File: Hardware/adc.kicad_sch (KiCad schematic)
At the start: 18 parts, among them U2 ADS1256IDBT, Y1 8MHz

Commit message: Version 0.1
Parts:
- removed R10, R12, R14, R15, R9: 100, Resistor_SMD:R_0805_2012Metric_Pad1.20x1.40mm_HandSolder, symbol Device:R
- removed R11, R13: 0, Resistor_SMD:R_0805_2012Metric_Pad1.20x1.40mm_HandSolder, symbol Device:R
- removed R7, R8: 10k, Resistor_SMD:R_0805_2012Metric_Pad1.20x1.40mm_HandSolder, symbol Device:R
- removed U2: ADS1256IDBT, ADS1256IDBT:SOP65P780X200-28N, symbol ADS1256:ADS1256IDBT
- removed Y1: 8MHz, Crystal:Crystal_SMD_3225-4Pin_3.2x2.5mm_HandSoldering, symbol Device:Crystal
- added U2: NAU7802SGI, symbol Nuvoton_-_NAU7802SGI:NAU7802SGI
- C10: value 18p -> 0.1uF; footprint Capacitor_SMD:C_0805_2012Metric_Pad1.18x1.45mm_HandSolder -> Capacitor_SMD:C_0603_1608Metric_Pad1.08x0.95mm_HandSolder
- C6: value 22u -> 1uF; footprint Capacitor_SMD:C_0805_2012Metric_Pad1.18x1.45mm_HandSolder -> Capacitor_SMD:C_0603_1608Metric_Pad1.08x0.95mm_HandSolder
- C7: value 100n -> 0.1uF; footprint Capacitor_SMD:C_0805_2012Metric_Pad1.18x1.45mm_HandSolder -> Capacitor_SMD:C_0603_1608Metric_Pad1.08x0.95mm_HandSolder
- C8: value 100p -> 0.1uF; footprint Capacitor_SMD:C_0805_2012Metric_Pad1.18x1.45mm_HandSolder -> Capacitor_SMD:C_0603_1608Metric_Pad1.08x0.95mm_HandSolder
- C9: value 18p -> 470pF; footprint Capacitor_SMD:C_0805_2012Metric_Pad1.18x1.45mm_HandSolder -> Capacitor_SMD:C_0603_1608Metric_Pad1.08x0.95mm_HandSolder
- R5, R6: value 49.9 -> 51; footprint Resistor_SMD:R_0805_2012Metric_Pad1.20x1.40mm_HandSolder -> Resistor_SMD:R_0603_1608Metric_Pad0.98x0.95mm_HandSolder
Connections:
- net +2V5 is gone; now on net AIN+: R5.1
- net +3V3: now also U2.15 (DVDD)
- net AIN-: now also R6.1
- net GND: now also C10.1, C6.1, C7.1, U2.7 (REFN), U2.8 (AVSS), U2.9 (DVSS); no longer C10.2, C9.1, R6.1
- net at C8.1, R5.2: now also U2.3 (VIN1P); no longer C6.1, C7.1
- net at C9.2: now also U2.4 (VIN2N)
- net at C6.2, C7.2: now also U2.1 (REFP); no longer C8.2, R6.2
- new net: C10.2, U2.6 (VBG)
- new net: C8.2, R6.2, U2.2 (VIN1N)
- new net: C9.1, U2.5 (VIN2P)
- new net SCL: U2.13 (SCLK)
- new net SDA: U2.14 (SDIO)
- no-connect marks 10 -> 0

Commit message: Readme + hole update
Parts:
- U2: footprint (none) -> Nuvoton-NAU7802SGI:Nuvoton-NAU7802SGI
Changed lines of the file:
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@@
     (property "Reference" "U2" (id 0) (at 157.48 90.17 0))
     (property "Value" "NAU7802SGI" (id 1) (at 157.48 92.71 0))
-    (property "Footprint" "" (id 2) (at 139.7 87.63 0)
+    (property "Footprint" "Nuvoton-NAU7802SGI:Nuvoton-NAU7802SGI" (id 2) (at 139.7 87.63 0)
       (effects (font (size 1.27 1.27)) (justify left) hide)
     )

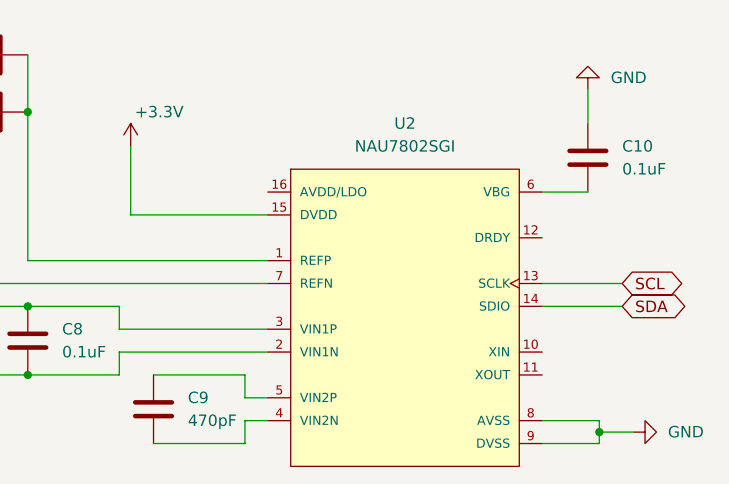
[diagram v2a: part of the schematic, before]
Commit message: removed TP561023, added footprint libraries
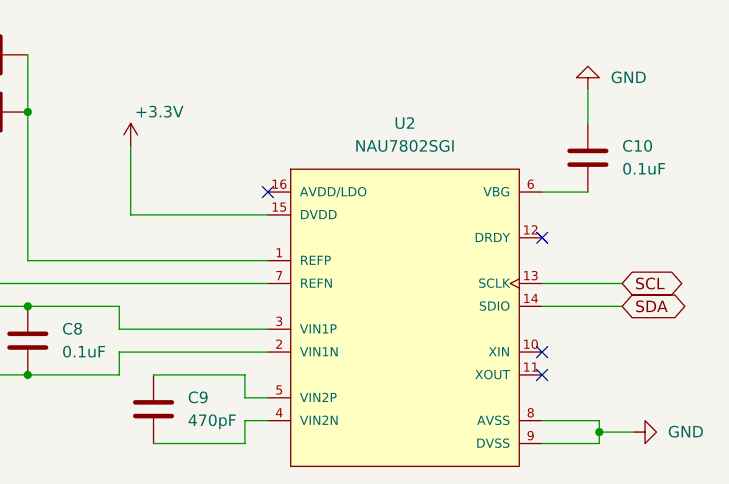
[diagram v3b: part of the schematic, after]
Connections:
- no-connect marks 0 -> 4
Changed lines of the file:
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@@
   (junction (at 107.95 82.55) (diameter 0) (color 0 0 0 0)
   )
+  (no_connect (at 172.72 102.87))
+  (no_connect (at 142.24 97.79))
+  (no_connect (at 172.72 118.11))
+  (no_connect (at 172.72 115.57))
   (wire (pts (xy 100.33 72.39) (xy 107.95 72.39))
     (stroke (width 0) (type default) (color 0 0 0 0))

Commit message: Updated power design
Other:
- note added: "This is 51ohms in Adafruits implementation"
- note added: "This was 0.1uF in Adafruit design"
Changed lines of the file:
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@@
     (stroke (width 0) (type default) (color 0 0 0 0))
+  )
+  (text "This was 0.1uF in \nAdafruit design" (at 125.73 113.03 0)
+    (effects (font (size 1.27 1.27)) (justify left bottom))
+  )
+  (text "This is 51ohms in \nAdafruits implementation" (at 100.33 130.81 0)
+    (effects (font (size 1.27 1.27)) (justify left bottom))
   )
   (global_label "SCL" (shape bidirectional) (at 181.61 107.95 0) (fields_autoplaced)

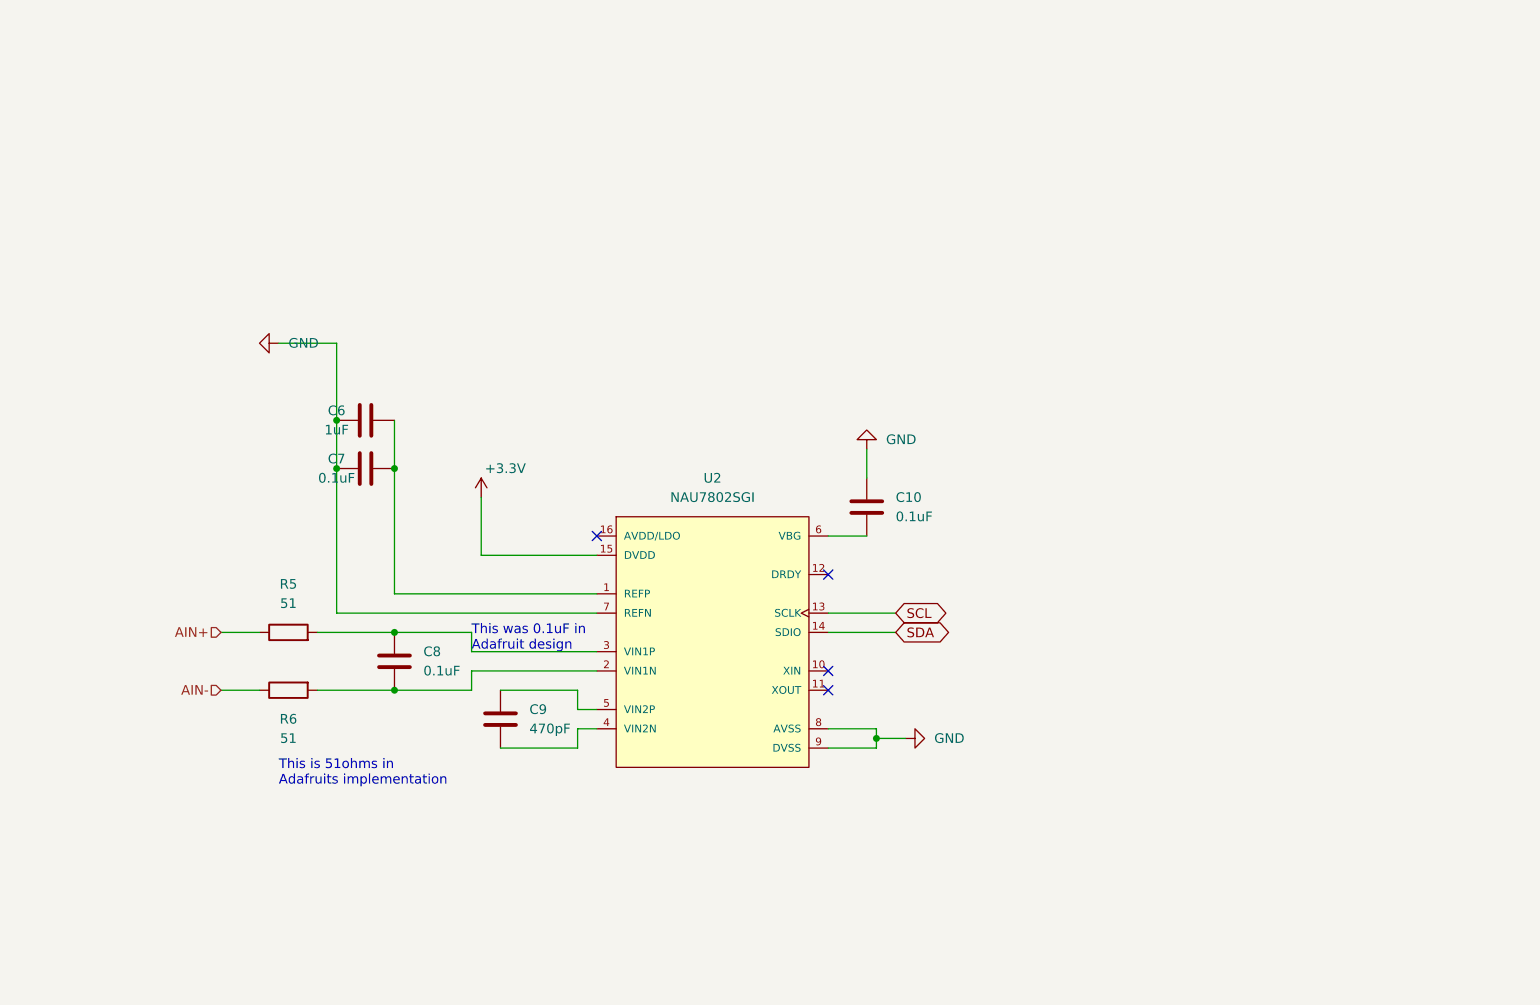
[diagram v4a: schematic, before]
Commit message: Version 0.6 - 4 layer version
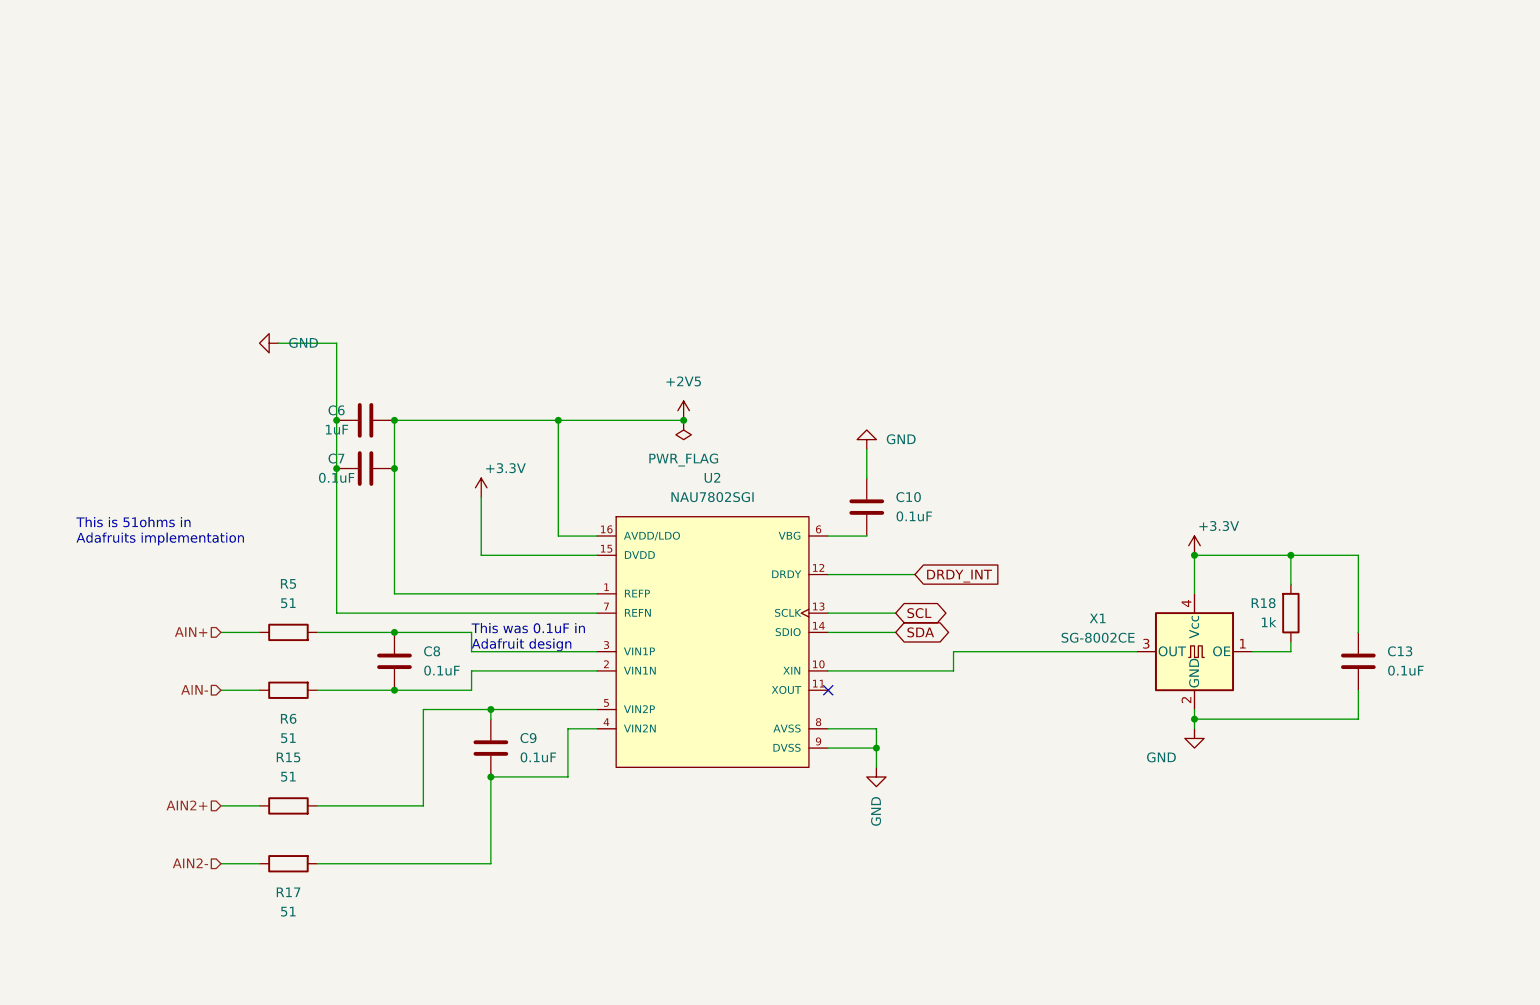
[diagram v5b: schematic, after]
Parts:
- added C13: 0.1uF, Capacitor_SMD:C_0603_1608Metric_Pad1.08x0.95mm_HandSolder, symbol Device:C
- added R15, R17: 51, Resistor_SMD:R_0603_1608Metric_Pad0.98x0.95mm_HandSolder, symbol Device:R
- added R18: 1k, Resistor_SMD:R_0603_1608Metric_Pad0.98x0.95mm_HandSolder, symbol Device:R
- added X1: SG-8002CE, Oscillator:Oscillator_SMD_SeikoEpson_SG8002CE-4Pin_3.2x2.5mm, symbol Oscillator:SG-8002CE
- C9: value 470pF -> 0.1uF
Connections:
- net +3V3: now also C13.1, R18.2, X1.4 (Vcc)
- net GND: now also C13.2, X1.2 (GND)
- net +2V5: now reaches C6.2, C7.2, U2.1 (REFP)
- net +2V5: now also U2.16 (AVDD/LDO)
- net at U2.10 (XIN): now also X1.3 (OUT)
- net DRDY_INT: now reaches U2.12 (DRDY)
- net at C9.2, U2.4 (VIN2N): now also R17.2
- net at C9.1, U2.5 (VIN2P): now also R15.2
- new net: R18.1, X1.1 (OE)
- new net AIN2+: R15.1
- new net AIN2-: R17.1
- no-connect marks 4 -> 1
